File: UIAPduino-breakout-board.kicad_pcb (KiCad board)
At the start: 2 copper layers, 56.6 x 54.1 mm, 14 parts, among them J1 Conn_01x20_Pin, J2 Conn_01x20_Socket, J3 Barrel_Jack_Switch, SW1 SW_SPDT_312, SW2 SW_SPDT_312, SW3 SW_Slide_DPDT, U3 L7805

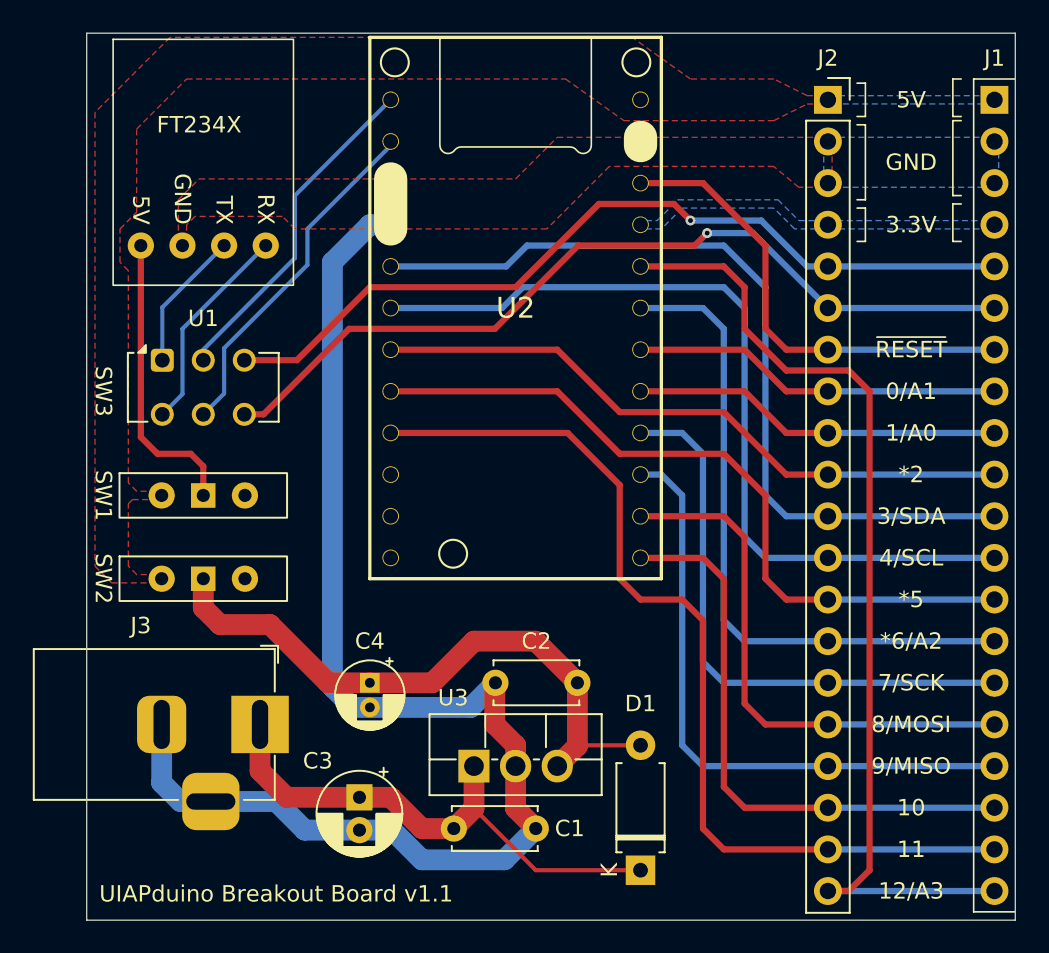
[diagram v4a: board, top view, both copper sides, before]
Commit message: シルク調整
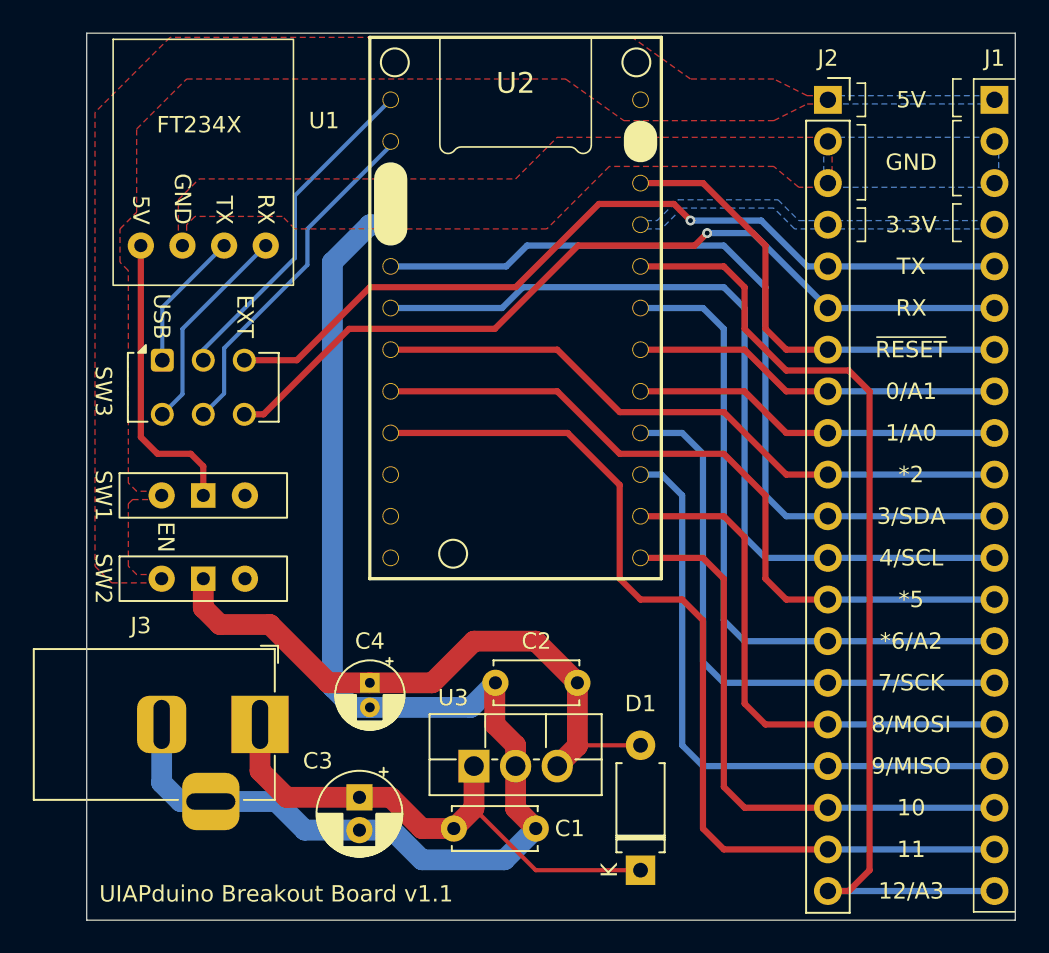
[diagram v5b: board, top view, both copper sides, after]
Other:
- board text added: "EN"
- board text added: "EXT"
- board text added: "RX"
- board text added: "TX"
- board text added: "USB"
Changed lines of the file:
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@@
 		(at 133.35 63.5)
 		(property "Reference" "U1"
-			(at 0 17.145 0)
+			(at 7.366 5.08 0)
 			(unlocked yes)
 			(layer "F.SilkS")
@@
 		(tags "UIAPduino Pro Micro CH32V003 V1.4")
 		(property "Reference" "U2"
-			(at 0 0 0)
+			(at 0 -13.716 0)
 			(layer "F.SilkS")
 			(effects
@@
 		)
 	)
+	(gr_text "USB"
+		(at 130.81 80.518 270)
+		(layer "F.SilkS")
+		(effects
+			(font
+				(size 1 1)
+				(thickness 0.1)
+			)
+		)
+	)
 	(gr_text "3/SDA"
 		(at 176.53 92.71 0)
@@
 		)
 	)
+	(gr_text "RX"
+		(at 176.53 80.01 0)
+		(layer "F.SilkS")
+		(effects
+			(font
+				(size 1 1)
+				(thickness 0.1)
+			)
+		)
+	)
 	(gr_text "11"
 		(at 176.53 113.03 0)
@@
 		)
 	)
+	(gr_text "EXT"
+		(at 135.89 80.518 -90)
+		(layer "F.SilkS")
+		(effects
+			(font
+				(size 1 1)
+				(thickness 0.1)
+			)
+		)
+	)
+	(gr_text "EN"
+		(at 131.064 93.98 270)
+		(layer "F.SilkS")
+		(effects
+			(font
+				(size 1 1)
+				(thickness 0.1)
+			)
+		)
+	)
 	(gr_text "9/MISO"
 		(at 176.53 107.95 0)
@@
 		(effects
 			(font
+				(size 1 1)
+				(thickness 0.1)
+			)
+		)
+	)
+	(gr_text "TX"
+		(at 176.53 77.47 0)
+		(layer "F.SilkS")
+		(effects
+			(font
